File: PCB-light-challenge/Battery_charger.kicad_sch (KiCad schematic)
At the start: 0 parts

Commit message: USB blad weg gehaald plus BQ25895 toegevoegd
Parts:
- added U1: BQ25895RTW, Package_DFN_QFN:Texas_S-PWQFN-N24_EP2.7x2.7mm_ThermalVias, symbol Battery_Management:BQ25895RTW
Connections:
- new net: U1.13 (BAT), U1.14 (BAT)
- new net: U1.15 (SYS), U1.16 (SYS)
- new net: U1.17 (PGND), U1.18 (PGND), U1.25 (PGND)
- new net: U1.19 (SW), U1.20 (SW)
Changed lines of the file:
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@@
 (kicad_sch (version 20230121) (generator eeschema)
   (paper "A4")
+  (symbol (lib_id "Battery_Management:BQ25895RTW") (at 146.05 96.52 0) (unit 1)
+    (in_bom yes) (on_board yes) (dnp no) (fields_autoplaced)
+    (property "Reference" "U1" (at 146.05 71.12 0)
+      (effects (font (size 1.27 1.27)))
+    )
+    (property "Value" "BQ25895RTW" (at 146.05 73.66 0)
+      (effects (font (size 1.27 1.27)))
+    )
+    (property "Footprint" "Package_DFN_QFN:Texas_S-PWQFN-N24_EP2.7x2.7mm_ThermalVias" (at 143.51 71.12 0)
+      (effects (font (size 1.27 1.27)) hide)
+    )
+    (property "Datasheet" "http://www.ti.com/lit/ds/symlink/bq25895.pdf" (at 140.97 76.2 0)
+      (effects (font (size 1.27 1.27)) hide)
+    )
+    (pin "1")
+    (pin "10")
+    (pin "11")
+    (pin "12")
+    (pin "13")
+    (pin "14")
+    (pin "15")
+    (pin "16")
+    (pin "17")
+    (pin "18")
+    (pin "19")
+    (pin "2")
+    (pin "20")
+    (pin "21")
+    (pin "22")
+    (pin "23")
+    (pin "24")
+    (pin "25")
+    (pin "3")
+    (pin "4")
+    (pin "5")
+    (pin "6")
+    (pin "7")
+    (pin "8")
+    (pin "9")
+    (instances
+      (project "PCB-light-challenge"
+        (path "/35573e8f-7834-430c-81d2-239f316c7834/1ee2b17a-9b36-4608-9d61-b871128bc979"
+          (reference "U1") (unit 1)
+        )
+      )
+    )
+  )
 )

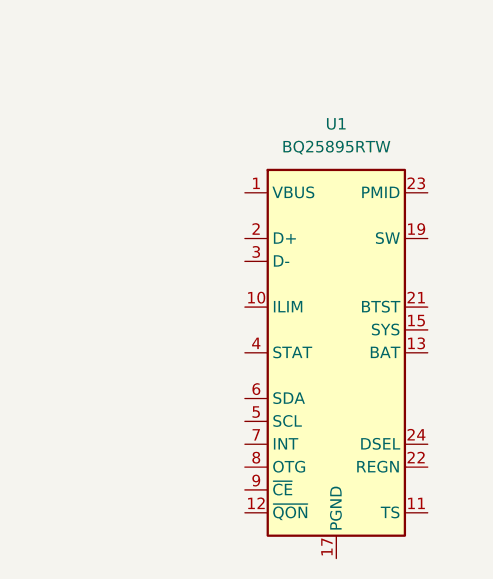
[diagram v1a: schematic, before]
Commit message: Batterij charger foorprint en symbol toegevoegd, BMS schema getekend , LDO symbol en footprint toegevoegd
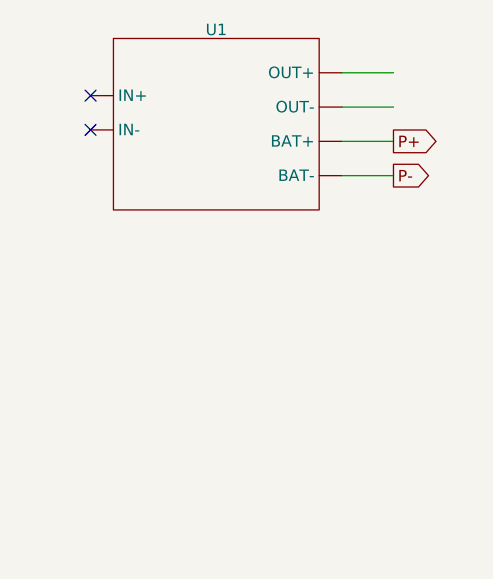
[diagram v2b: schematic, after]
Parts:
- removed U1: BQ25895RTW, Package_DFN_QFN:Texas_S-PWQFN-N24_EP2.7x2.7mm_ThermalVias, symbol Battery_Management:BQ25895RTW
- added U1: ~, BMS:bms, symbol TP4056 USB-C Li-ion charger:TP4056_USB-C_charger
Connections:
- new net P+: U1. (OUT-)
- new net P-: U1. (OUT-)
- no-connect marks 0 -> 2
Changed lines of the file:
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@@
 (kicad_sch (version 20230121) (generator eeschema)
   (paper "A4")
-  (symbol (lib_id "Battery_Management:BQ25895RTW") (at 146.05 96.52 0) (unit 1)
+  (no_connect (at 118.745 67.945))
+  (no_connect (at 118.745 71.755))
+  (wire (pts (xy 146.685 73.025) (xy 152.4 73.025))
+    (stroke (width 0) (type default))
+  )
+  (wire (pts (xy 146.685 65.405) (xy 152.4 65.405))
+    (stroke (width 0) (type default))
+  )
+  (wire (pts (xy 146.685 76.835) (xy 152.4 76.835))
+    (stroke (width 0) (type default))
+  )
+  (wire (pts (xy 146.685 69.215) (xy 152.4 69.215))
+    (stroke (width 0) (type default))
+  )
+  (global_label "P+" (shape output) (at 152.4 73.025 0) (fields_autoplaced)
+    (effects (font (size 1.27 1.27)) (justify left))
+    (property "Intersheetrefs" "${INTERSHEET_REFS}" (at 158.1482 73.025 0)
+      (effects (font (size 1.27 1.27)) (justify left) hide)
+    )
+  )
+  (global_label "P-" (shape output) (at 152.4 76.835 0) (fields_autoplaced)
+    (effects (font (size 1.27 1.27)) (justify left))
+    (property "Intersheetrefs" "${INTERSHEET_REFS}" (at 158.1482 76.835 0)
+      (effects (font (size 1.27 1.27)) (justify left) hide)
+    )
+  )
+  (symbol (lib_id "TP4056 USB-C Li-ion charger:TP4056_USB-C_charger") (at 132.715 64.135 0) (unit 1)
     (in_bom yes) (on_board yes) (dnp no) (fields_autoplaced)
-    (property "Reference" "U1" (at 146.05 71.12 0)
+    (property "Reference" "U1" (at 132.715 60.6331 0)
       (effects (font (size 1.27 1.27)))
     )
-    (property "Value" "BQ25895RTW" (at 146.05 73.66 0)
+    (property "Value" "~" (at 137.795 64.135 0)
       (effects (font (size 1.27 1.27)))
     )
-    (property "Footprint" "Package_DFN_QFN:Texas_S-PWQFN-N24_EP2.7x2.7mm_ThermalVias" (at 143.51 71.12 0)
+    (property "Footprint" "BMS:bms" (at 137.795 64.135 0)
       (effects (font (size 1.27 1.27)) hide)
     )
-    (property "Datasheet" "http://www.ti.com/lit/ds/symlink/bq25895.pdf" (at 140.97 76.2 0)
+    (property "Datasheet" "" (at 137.795 64.135 0)
       (effects (font (size 1.27 1.27)) hide)
     )
-    (pin "1")
-    (pin "10")
-    (pin "11")
-    (pin "12")
-    (pin "13")
-    (pin "14")
-    (pin "15")
-    (pin "16")
-    (pin "17")
-    (pin "18")
-    (pin "19")
-    (pin "2")
-    (pin "20")
-    (pin "21")
-    (pin "22")
-    (pin "23")
-    (pin "24")
-    (pin "25")
-    (pin "3")
-    (pin "4")
-    (pin "5")
-    (pin "6")
-    (pin "7")
-    (pin "8")
-    (pin "9")
+    (pin "")
+    (pin "")
+    (pin "")
+    (pin "")
+    (pin "")
+    (pin "")
     (instances
       (project "PCB-light-challenge"

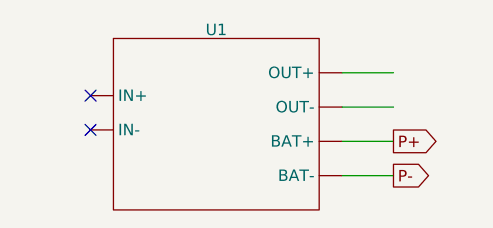
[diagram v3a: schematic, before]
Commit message: RP2040  pinout toegevoegd   met naam
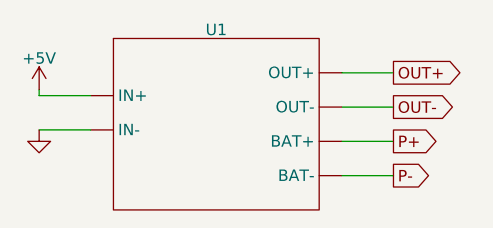
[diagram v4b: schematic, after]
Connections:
- new net +5V: U1. (OUT-)
- new net GND: U1. (OUT-)
- new net OUT+: U1. (OUT-)
- new net OUT-: U1. (OUT-)
- no-connect marks 2 -> 0
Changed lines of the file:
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@@
 (kicad_sch (version 20230121) (generator eeschema)
   (paper "A4")
-  (no_connect (at 118.745 67.945))
-  (no_connect (at 118.745 71.755))
   (wire (pts (xy 146.685 73.025) (xy 152.4 73.025))
+    (stroke (width 0) (type default))
+  )
+  (wire (pts (xy 113.03 67.31) (xy 113.03 67.945))
+    (stroke (width 0) (type default))
+  )
+  (wire (pts (xy 118.745 67.945) (xy 113.03 67.945))
+    (stroke (width 0) (type default))
+  )
+  (wire (pts (xy 113.03 71.755) (xy 118.745 71.755))
     (stroke (width 0) (type default))
   )
@@
     (property "Intersheetrefs" "${INTERSHEET_REFS}" (at 158.1482 76.835 0)
       (effects (font (size 1.27 1.27)) (justify left) hide)
+    )
+  )
+  (global_label "OUT-" (shape output) (at 152.4 69.215 0) (fields_autoplaced)
+    (effects (font (size 1.27 1.27)) (justify left))
+    (property "Intersheetrefs" "${INTERSHEET_REFS}" (at 160.5068 69.215 0)
+      (effects (font (size 1.27 1.27)) (justify left) hide)
+    )
+  )
+  (global_label "OUT+" (shape output) (at 152.4 65.405 0) (fields_autoplaced)
+    (effects (font (size 1.27 1.27)) (justify left))
+    (property "Intersheetrefs" "${INTERSHEET_REFS}" (at 160.5068 65.405 0)
+      (effects (font (size 1.27 1.27)) (justify left) hide)
+    )
+  )
+  (symbol (lib_id "power:+5V") (at 113.03 67.31 0) (unit 1)
+    (in_bom yes) (on_board yes) (dnp no) (fields_autoplaced)
+    (property "Reference" "#PWR014" (at 113.03 71.12 0)
+      (effects (font (size 1.27 1.27)) hide)
+    )
+    (property "Value" "+5V" (at 113.03 63.8081 0)
+      (effects (font (size 1.27 1.27)))
+    )
+    (property "Footprint" "" (at 113.03 67.31 0)
+      (effects (font (size 1.27 1.27)) hide)
+    )
+    (property "Datasheet" "" (at 113.03 67.31 0)
+      (effects (font (size 1.27 1.27)) hide)
+    )
+    (pin "1")
+    (instances
+      (project "PCB-light-challenge"
+        (path "/35573e8f-7834-430c-81d2-239f316c7834/1ee2b17a-9b36-4608-9d61-b871128bc979"
+          (reference "#PWR014") (unit 1)
+        )
+      )
     )
   )
@@
         )
       )
+    )
+  )
+  (symbol (lib_id "power:GND") (at 113.03 71.755 0) (unit 1)
+    (in_bom yes) (on_board yes) (dnp no) (fields_autoplaced)
+    (property "Reference" "#PWR015" (at 113.03 78.105 0)
+      (effects (font (size 1.27 1.27)) hide)
+    )
+    (property "Value" "GND" (at 113.03 75.8905 0)
+      (effects (font (size 1.27 1.27)) hide)
+    )
+    (property "Footprint" "" (at 113.03 71.755 0)
+      (effects (font (size 1.27 1.27)) hide)
+    )
+    (property "Datasheet" "" (at 113.03 71.755 0)
+      (effects (font (size 1.27 1.27)) hide)
+    )
+    (pin "1")
+    (instances
+      (project "PCB-light-challenge"
+        (path "/35573e8f-7834-430c-81d2-239f316c7834/1ee2b17a-9b36-4608-9d61-b871128bc979"
+          (reference "#PWR015") (unit 1)
+        )
+      )
